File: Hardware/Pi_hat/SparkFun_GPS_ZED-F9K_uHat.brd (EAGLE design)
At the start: 65 x 30.5 mm, 41 parts, among them J4 U.FL, J7 RASPBERRYPI-40-PIN-GPIO_PTH_N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, U1 UBLOX_ZED_F9K, U3 TRIPLE_BUFFER_74LVC3G07

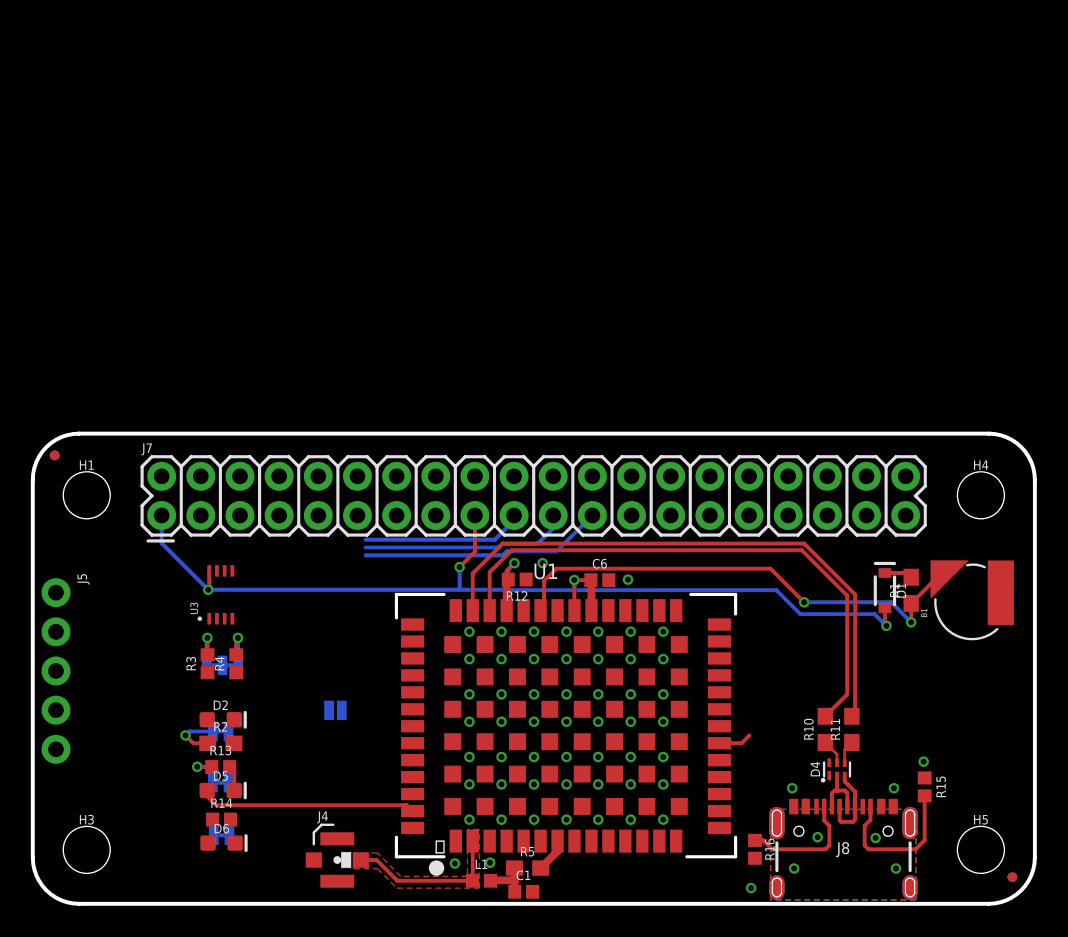
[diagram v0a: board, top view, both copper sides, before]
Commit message: Adds trace work for piHat version - still needs silk
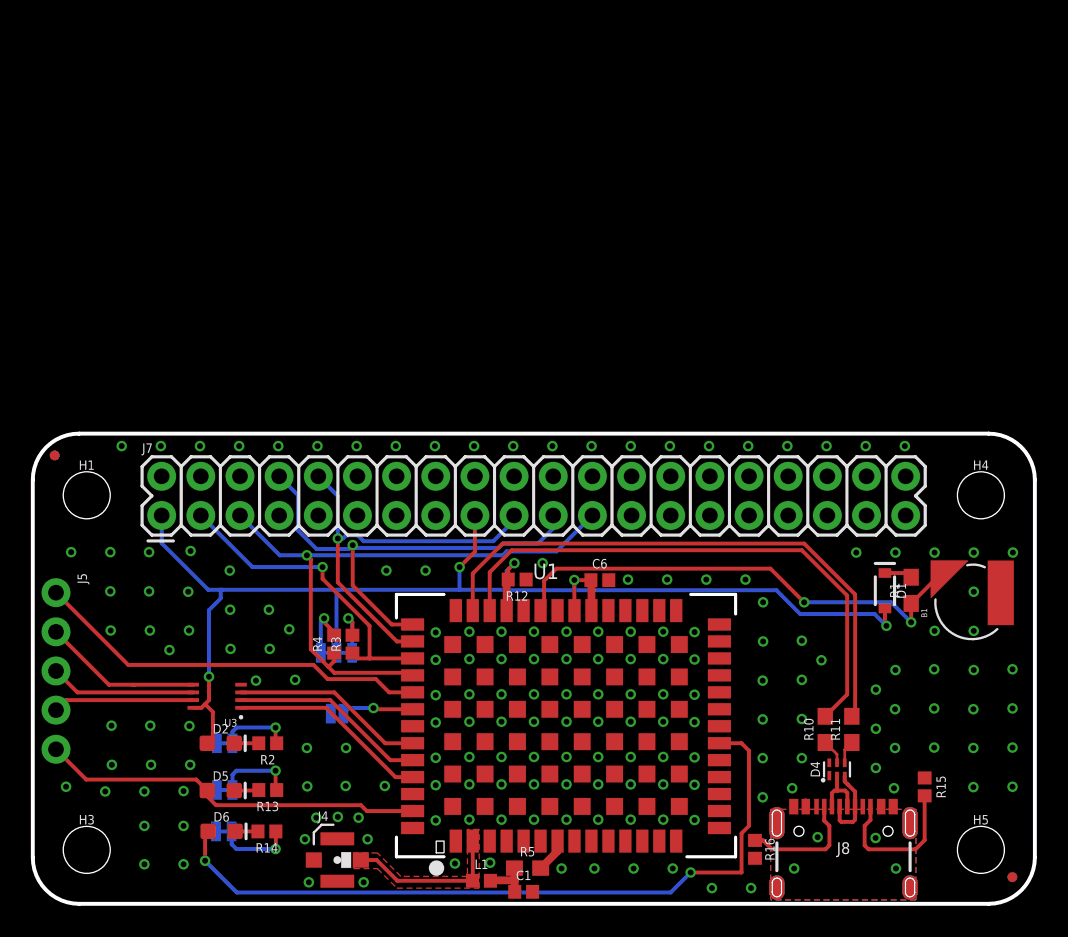
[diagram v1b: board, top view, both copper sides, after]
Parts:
- R2: value 1k -> 1KOHM-0402-1/16W-1%; device SparkFun-Resistors:0603 -> SparkFun-Resistors:0402
- moved R3 9.48 mm to (20.7, 16.8)
- moved JP2 7.44 mm to (19.7, 16.3), turned to 0 degrees
- moved R4 6.48 mm to (19.5, 16.8)
- moved U3 6.19 mm to (13.5, 12.7), turned to 180 degrees
- moved R13 3.39 mm to (15.2, 7.38), turned to 180 degrees
- moved R2 3.05 mm to (15.2, 10.4), turned to 180 degrees
- moved R14 3.04 mm to (15.2, 4.70), turned to 180 degrees
- moved D2 1.52 mm to (12.2, 10.4)
- moved PWR 0.80 mm to (12.4, 10.4), turned to 180 degrees
- moved D6 0.76 mm to (12.2, 4.70)
- moved PPS 0.54 mm to (12.4, 7.38), turned to 180 degrees
- moved RTK 0.29 mm to (12.4, 4.70), turned to 180 degrees
- moved JP1 0.24 mm to (19.7, 12.3), turned to 0 degrees
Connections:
- net !RESET_IN: now also U3.P3; no longer U3.P1
- net !RESET_OUT: now also J5.4; no longer J5.2
- net !SAFEBOOT_IN: now also J5.3; no longer U1.P50
- net !SAFEBOOT_OUT: now also U1.P50; no longer J5.4
- net INT_IN: now also U3.P1; no longer U3.P3
- net INT_OUT: now also J5.2; no longer J5.1
- net PPS: now also J5.5; no longer J5.3
- net TX_READY: now also J5.1; no longer J5.5
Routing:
- net RTK_STAT: track 2.15 -> 48.4 mm, vias 0 -> 2
- net TX_READY: track 0.00 -> 25.8 mm
- net SCL/CLK: track 15.8 -> 39.6 mm, vias 0 -> 1
- net SDA/!CS: track 0.00 -> 20.5 mm, vias 0 -> 1
- net TXO/MISO: track 13.5 -> 30.2 mm, vias 0 -> 1
- net RXI/MOSI: track 10.5 -> 26.4 mm, vias 0 -> 1
- net 3.3V: track 69.9 -> 84.4 mm
- net INT_IN: track 0.00 -> 13.0 mm
- net !SAFEBOOT_OUT: track 0.00 -> 12.7 mm
- net !RESET_IN: track 0.00 -> 12.5 mm
- net PPS: track 14.1 -> 25.0 mm
- net INT_OUT: track 0.00 -> 10.3 mm
- net !SAFEBOOT_IN: track 0.00 -> 9.48 mm
- net !RESET_OUT: track 0.00 -> 9.17 mm
- net N$22: track 0.00 -> 4.96 mm, vias 0 -> 1
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
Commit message: Replaces micro hat with regular hat
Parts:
- removed FD1, FD2, FD3, FD4: FIDUCIALUFIDUCIAL, SparkFun-Aesthetics:FIDUCIAL-MICRO
- removed H1, H4: STAND-OFFTIGHT, SparkFun-Hardware:STAND-OFF-TIGHT
- removed J7: RASPBERRYPI-40-PIN-GPIO_PTH_NO_SHROUD, SparkFun-Connectors:2X20
- added FD10, FD11, FD12, FD9: FIDUCIALUFIDUCIAL, SparkFun-Aesthetics:FIDUCIAL-MICRO
- added H11, H12: STAND-OFFTIGHT, SparkFun-Hardware:STAND-OFF-TIGHT
- added J2: RASPBERRYPI-40-PIN-GPIO_PTH_NO_SHROUD, SparkFun-Connectors:2X20
- moved U3 29.5 mm to (13.0, 42.2)
- moved J5 28.5 mm to (2.01, 48.6)
- moved B1 24.6 mm to (57.9, 44.0)
- moved R1 24.6 mm to (53.9, 44.7)
- moved D1 24.6 mm to (52.2, 44.7)
- moved JP1 20.5 mm to (16.9, 32.7)
- moved R3 20.5 mm to (17.9, 37.2)
- moved R4 20.5 mm to (16.8, 37.2)
- moved C6 20.5 mm to (34.0, 41.3)
- moved J4 20.5 mm to (17.0, 23.2)
- moved JP2 20.5 mm to (16.9, 36.6)
- moved L1 20.5 mm to (26.3, 21.8)
- moved R5 20.5 mm to (29.3, 22.6)
- moved R12 20.5 mm to (28.6, 41.4)
- moved U1 20.4 mm to (32.5, 32.0)
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- renumbered H3 to H9, H5 to H10
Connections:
- removed net N$10: J7.2, J7.4
- new net 5V: J2.2, J2.4
- net 3.3V: now also J2.1, J2.17; no longer J7.1, J7.17
- net GND: now also J2.14, J2.20, J2.25, J2.30, J2.34, J2.39, J2.6, J2.9; no longer J7.14, J7.20, J7.25, J7.30, J7.34, J7.39, J7.6, J7.9
- net RXI/MOSI: no longer J7.10, J7.19
- net SCL/CLK: no longer J7.23, J7.5
- net SDA/!CS: no longer J7.3
- net TXO/MISO: no longer J7.21, J7.8
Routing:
- net 3.3V: track 84.4 -> 0.00 mm, vias 5 -> 0
- net RTK_STAT: track 48.4 -> 0.00 mm, vias 2 -> 0
- net SCL/CLK: track 39.6 -> 0.00 mm, vias 1 -> 0
- net DPLUS: track 37.4 -> 0.00 mm
- net DMINUS: track 35.9 -> 0.00 mm
- net V_BATT: track 32.1 -> 0.00 mm, vias 2 -> 0
- net TXO/MISO: track 30.2 -> 0.00 mm, vias 1 -> 0
- net RXI/MOSI: track 26.4 -> 0.00 mm, vias 1 -> 0
- net TX_READY: track 25.8 -> 0.00 mm
- net PPS: track 25.0 -> 0.00 mm
- net SDA/!CS: track 20.5 -> 0.00 mm, vias 1 -> 0
- net INT_IN: track 13.0 -> 0.00 mm
- net !SAFEBOOT_OUT: track 12.7 -> 0.00 mm
- net !RESET_IN: track 12.5 -> 0.00 mm
- net RF_IN: track 10.4 -> 0.00 mm
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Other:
- board size 65 x 30.5 mm -> 65 x 56.5 mm
